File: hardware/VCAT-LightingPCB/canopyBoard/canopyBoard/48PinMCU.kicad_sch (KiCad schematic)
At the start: 34 parts, among them J17 SWD_Header, J18 SWD, SW13 Reset, SW14 SW_SPDT, U16 STM32G473CETx, Y6 Crystal

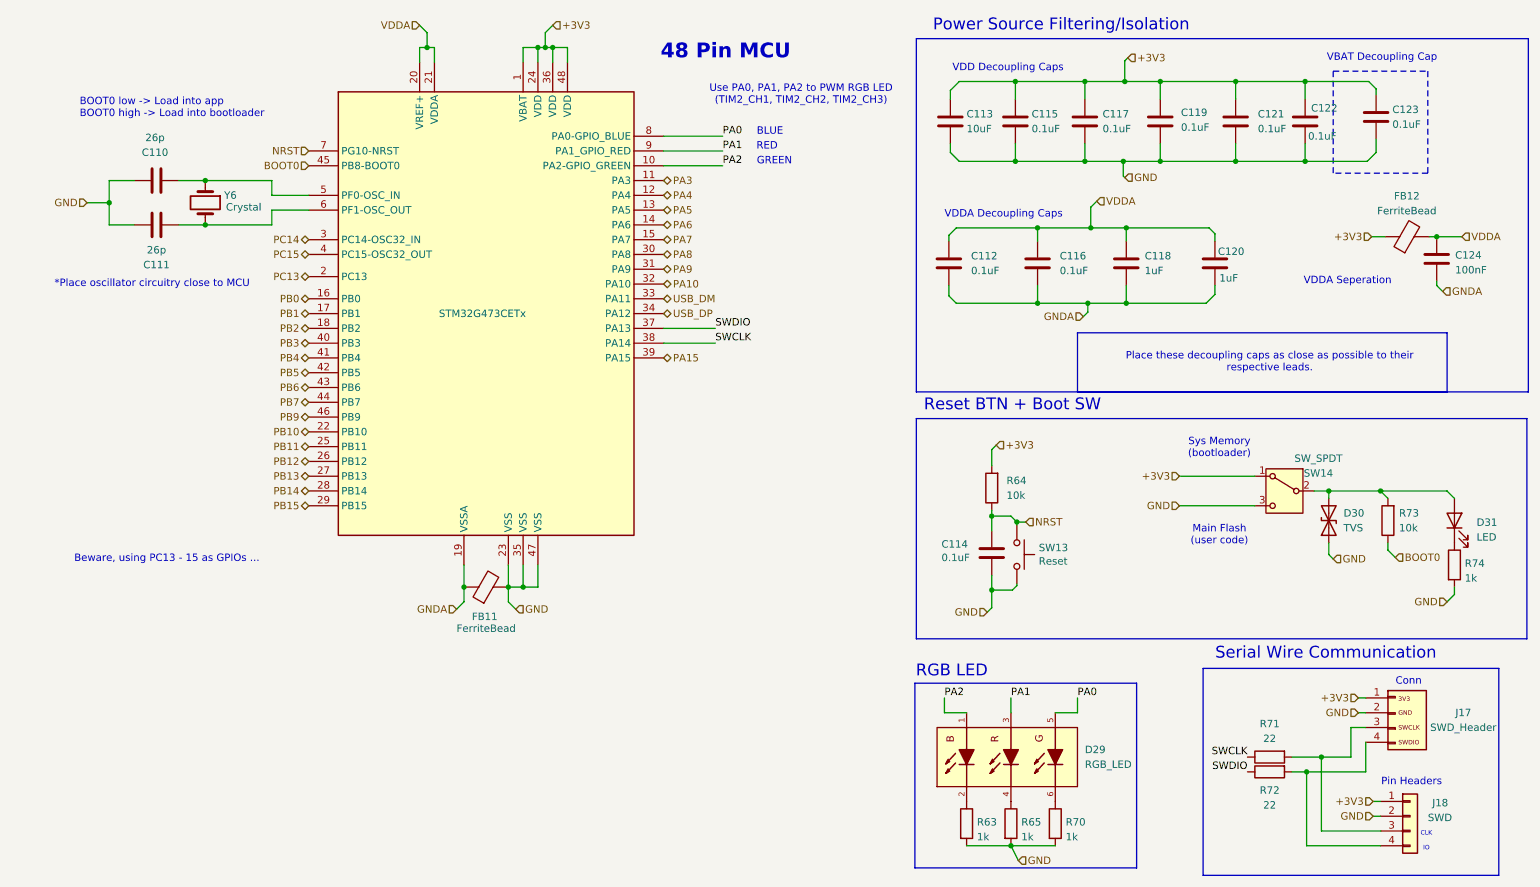
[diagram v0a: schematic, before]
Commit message: Untrack KiCad .history, convert KiCAD-Sharepoint to a submodule, remove LightsPCB
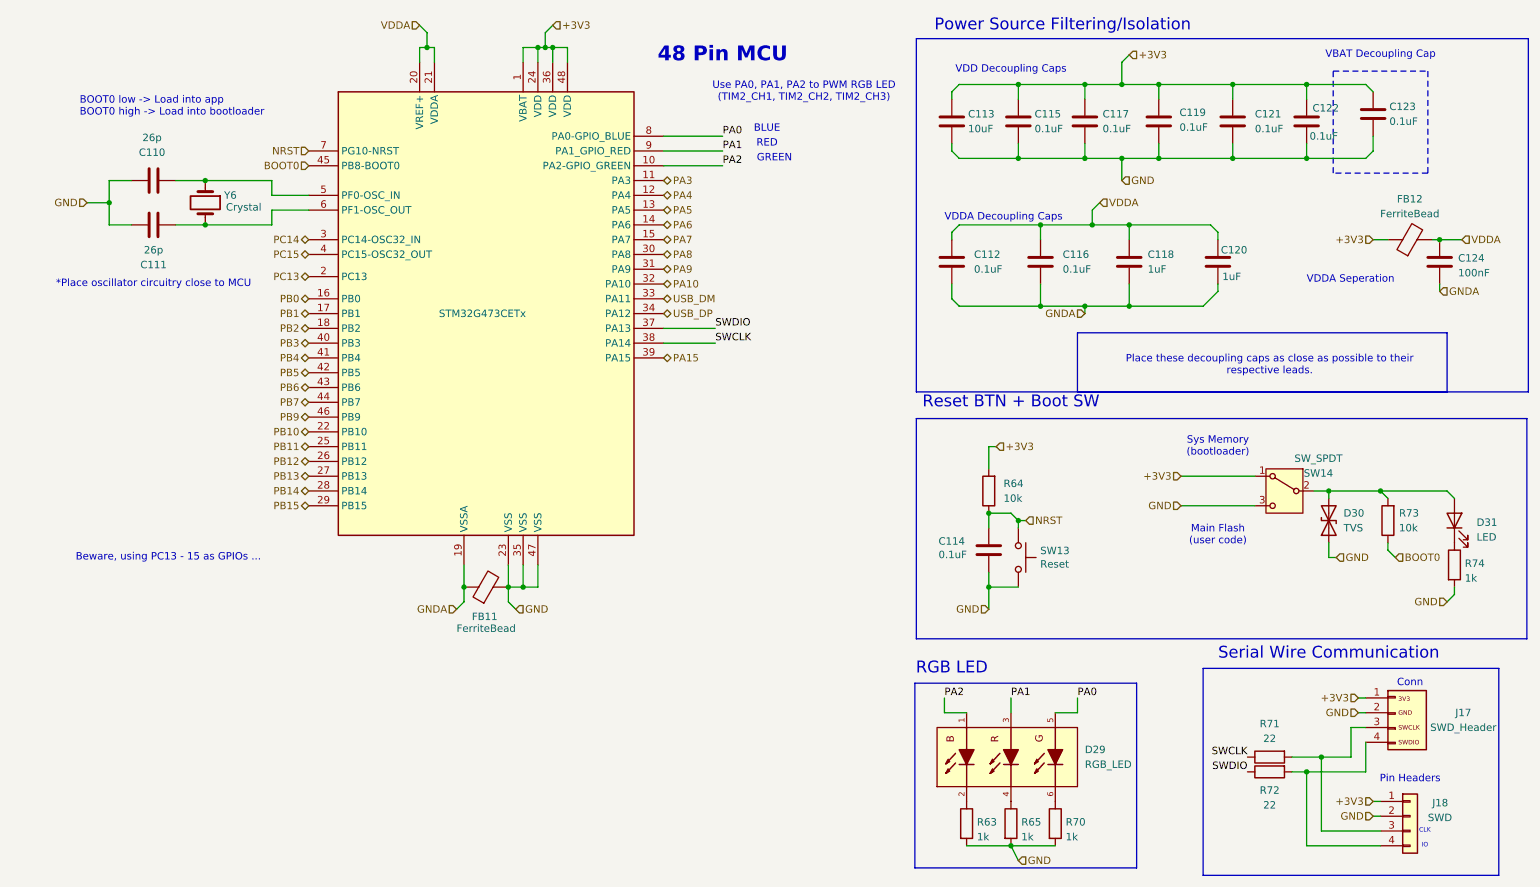
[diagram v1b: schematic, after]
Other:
- moved on the sheet: C110, C111, C112, C114, C115, C116, C118, C120, C121, C123, C124, FB12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
